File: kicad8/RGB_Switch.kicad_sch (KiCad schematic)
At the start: 0 parts

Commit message: Added: Stepped CAPS_LOCK and Split backspace
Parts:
- added Q1: WSD4070DN, PCM_marbastlib-various:PDFN3.3x3.3_EP, symbol PCM_marbastlib-various:WSD4070DN
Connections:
- new net: Q1.1 (S), Q1.2 (S), Q1.3 (S)
- new net: Q1.5 (D), Q1.6 (D), Q1.7 (D), Q1.8 (D), Q1.9 (D)
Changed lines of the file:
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@@
 	(generator_version "8.0")
 	(paper "A4")
+	(symbol
+		(lib_id "PCM_marbastlib-various:WSD4070DN")
+		(at 33.02 26.67 0)
+		(unit 1)
+		(exclude_from_sim no)
+		(in_bom yes)
+		(on_board yes)
+		(dnp no)
+		(fields_autoplaced yes)
+		(property "Reference" "Q1"
+			(at 39.37 25.3999 0)
+			(effects
+				(font
+					(size 1.27 1.27)
+				)
+				(justify left)
+			)
+		)
+		(property "Value" "WSD4070DN"
+			(at 39.37 27.9399 0)
+			(effects
+				(font
+					(size 1.27 1.27)
+				)
+				(justify left)
+			)
+		)
+		(property "Footprint" "PCM_marbastlib-various:PDFN3.3x3.3_EP"
+			(at 38.1 24.13 0)
+			(effects
+				(font
+					(size 1.27 1.27)
+				)
+				(hide yes)
+			)
+		)
+		(property "Datasheet" "https://wmsc.lcsc.com/wmsc/upload/file/pdf/v2/lcsc/2008211234_Winsok-Semicon-WSD4070DN_C719095.pdf"
+			(at 33.02 39.37 0)
+			(effects
+				(font
+					(size 1.27 1.27)
+				)
+				(hide yes)
+			)
+		)
+		(property "Description" "NMOS 40V 4.5 mOhm 68A"
+			(at 33.02 26.67 0)
+			(effects
+				(font
+					(size 1.27 1.27)
+				)
+				(hide yes)
+			)
+		)
+		(pin "2"
+		)
+		(pin "3"
+		)
+		(pin "5"
+		)
+		(pin "4"
+		)
+		(pin "7"
+		)
+		(pin "1"
+		)
+		(pin "8"
+		)
+		(pin "6"
+		)
+		(pin "9"
+		)
+		(instances
+			(project ""
+				(path "/4d291fcf-fdf2-46ba-aa57-60bc75f9cc32/7638bbfc-5c02-4928-8821-3938de956d68"
+					(reference "Q1")
+					(unit 1)
+				)
+			)
+		)
+	)
 )

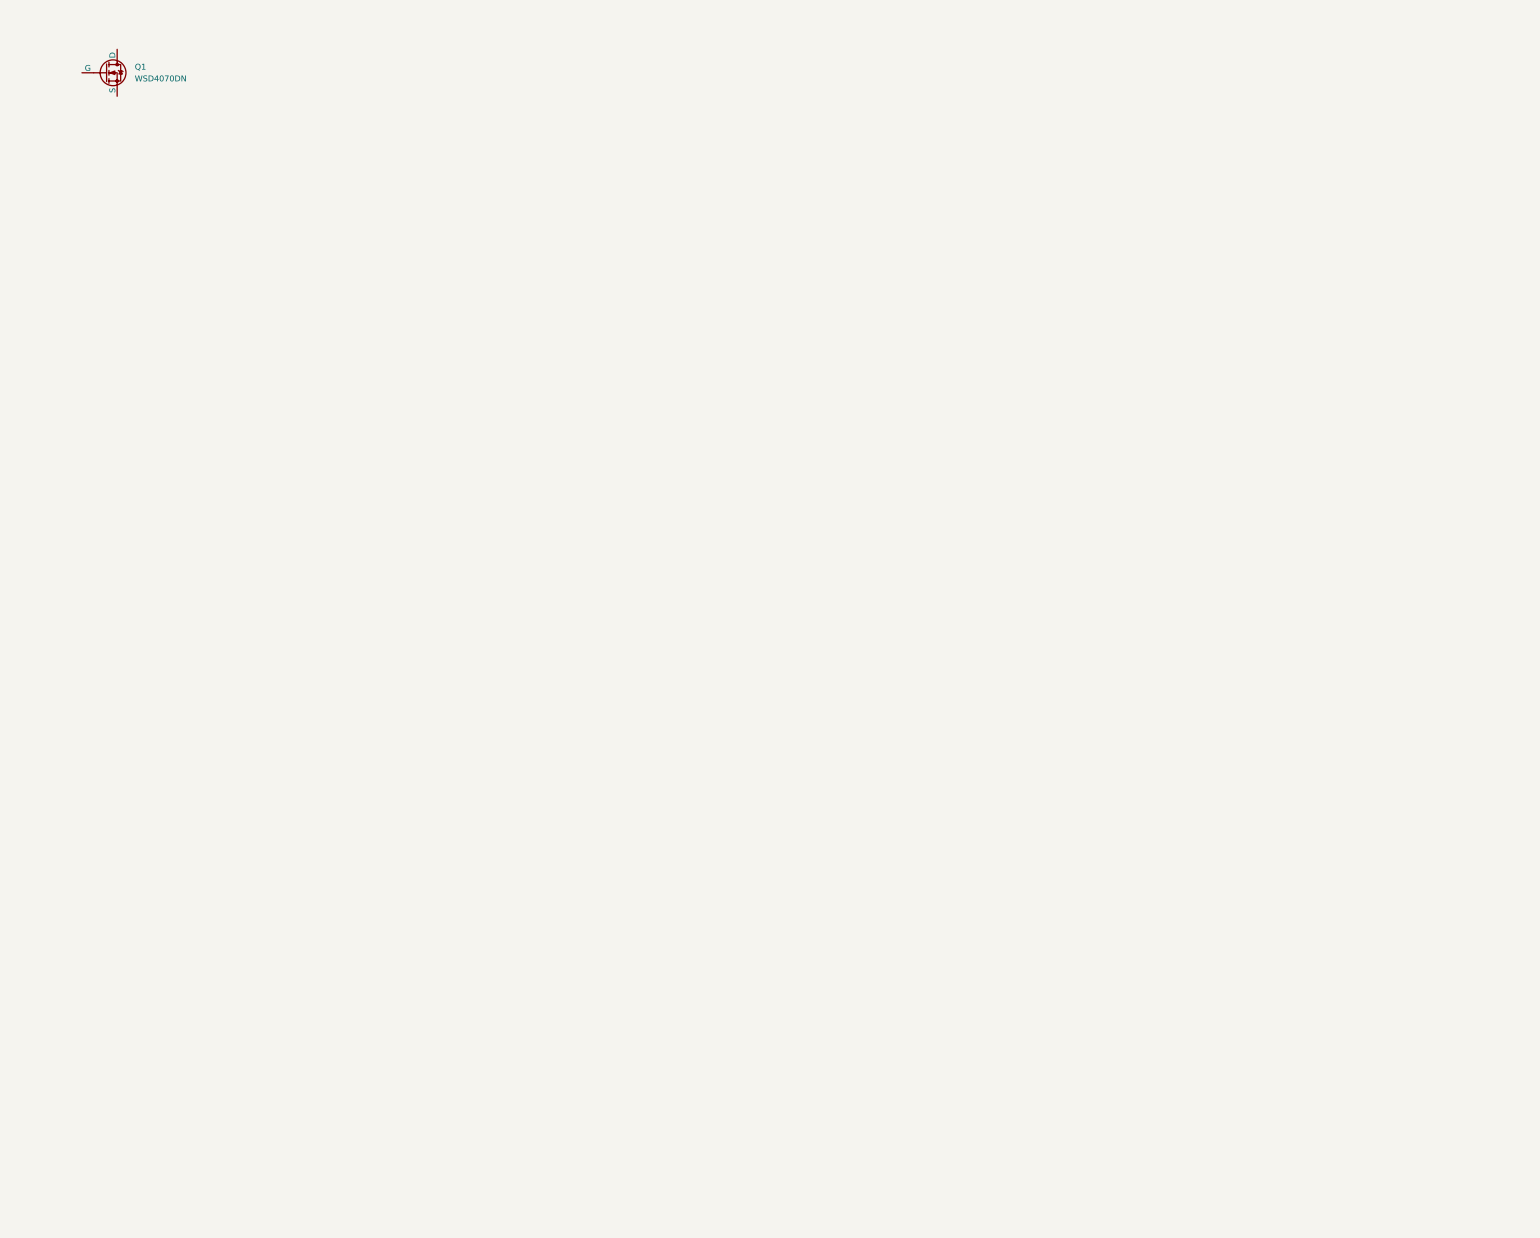
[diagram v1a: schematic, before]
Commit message: Finished: Wiring for the Switch matrix, Underglow RGB and Per-key RGb
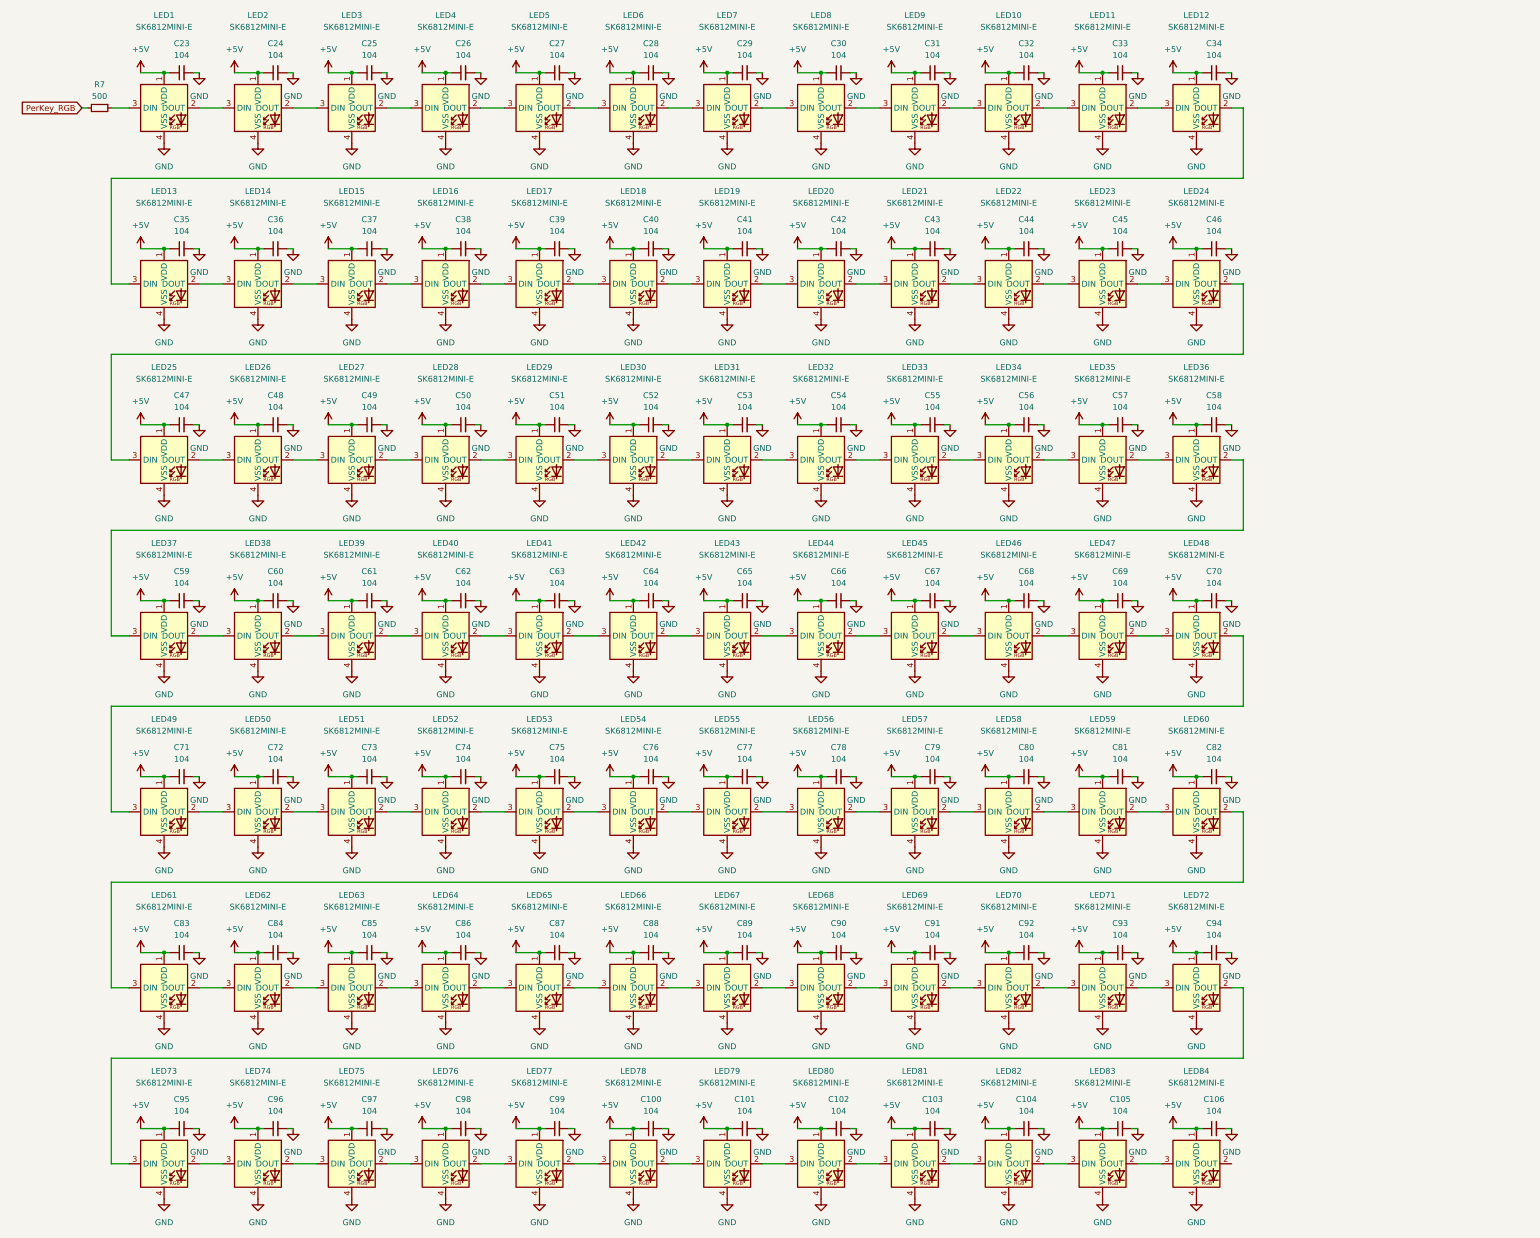
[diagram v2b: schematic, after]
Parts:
- removed Q1: WSD4070DN, PCM_marbastlib-various:PDFN3.3x3.3_EP, symbol PCM_marbastlib-various:WSD4070DN
- added C100, C101, C102, C103, C104, C105, C106, C23, C24, C25, C26, C27, C28, C29, C30, C31, C32, C33, C34, C35, C36, C37, C38, C39, C40, C41, C42, C43, C44, C45, C46, C47, C48, C49, C50, C51, C52, C53, C54, C55, C56, C57, C58, C59, C60, C61, C62, C63, C64, C65, C66, C67, C68, C69, C70, C71, C72, C73, C74, C75, C76, C77, C78, C79, C80, C81, C82, C83, C84, C85, C86, C87, C88, C89, C90, C91, C92, C93, C94, C95, C96, C97, C98, C99: 104, Diode_SMD:D_SOD-123, symbol Device:C_Small
- added LED1, LED10, LED11, LED12, LED13, LED14, LED15, LED16, LED17, LED18, LED19, LED2, LED20, LED21, LED22, LED23, LED24, LED25, LED26, LED27, LED28, LED29, LED3, LED30, LED31, LED32, LED33, LED34, LED35, LED36, LED37, LED38, LED39, LED4, LED40, LED41, LED42, LED43, LED44, LED45, LED46, LED47, LED48, LED49, LED5, LED50, LED51, LED52, LED53, LED54, LED55, LED56, LED57, LED58, LED59, LED6, LED60, LED61, LED62, LED63, LED64, LED65, LED66, LED67, LED68, LED69, LED7, LED70, LED71, LED72, LED73, LED74, LED75, LED76, LED77, LED78, LED79, LED8, LED80, LED81, LED82, LED83, LED84, LED9: SK6812MINI-E, PCM_marbastlib-various:LED_6028R, symbol PCM_marbastlib-various:SK6812MINI-E
- added R7: 500, Diode_SMD:D_SOD-123, symbol Device:R_Small
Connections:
- new net: LED73.2 (DOUT), LED74.3 (DIN)
- new net: LED72.2 (DOUT), LED73.3 (DIN)
- new net: LED45.2 (DOUT), LED46.3 (DIN)
- new net: LED44.2 (DOUT), LED45.3 (DIN)
- new net: LED79.2 (DOUT), LED80.3 (DIN)
- new net: LED78.2 (DOUT), LED79.3 (DIN)
- new net: LED42.2 (DOUT), LED43.3 (DIN)
- new net: LED41.2 (DOUT), LED42.3 (DIN)
- new net: LED35.2 (DOUT), LED36.3 (DIN)
- new net: LED34.2 (DOUT), LED35.3 (DIN)
- new net: LED15.2 (DOUT), LED16.3 (DIN)
- new net: LED14.2 (DOUT), LED15.3 (DIN)
- new net: LED5.2 (DOUT), LED6.3 (DIN)
- new net: LED4.2 (DOUT), LED5.3 (DIN)
- new net: LED37.2 (DOUT), LED38.3 (DIN)
- new net: LED36.2 (DOUT), LED37.3 (DIN)
- new net: LED17.2 (DOUT), LED18.3 (DIN)
- new net: LED16.2 (DOUT), LED17.3 (DIN)
- new net: LED50.2 (DOUT), LED51.3 (DIN)
- new net: LED49.2 (DOUT), LED50.3 (DIN)
- new net: LED74.2 (DOUT), LED75.3 (DIN)
- new net: LED48.2 (DOUT), LED49.3 (DIN)
- new net: LED47.2 (DOUT), LED48.3 (DIN)
- new net: LED38.2 (DOUT), LED39.3 (DIN)
- new net: LED75.2 (DOUT), LED76.3 (DIN)
- new net: LED81.2 (DOUT), LED82.3 (DIN)
- new net: LED80.2 (DOUT), LED81.3 (DIN)
- new net: LED23.2 (DOUT), LED24.3 (DIN)
- new net: LED22.2 (DOUT), LED23.3 (DIN)
- new net: LED70.2 (DOUT), LED71.3 (DIN)
- new net: LED69.2 (DOUT), LED70.3 (DIN)
- new net: LED66.2 (DOUT), LED67.3 (DIN)
- new net: LED65.2 (DOUT), LED66.3 (DIN)
- new net: LED10.2 (DOUT), LED11.3 (DIN)
- new net: LED10.3 (DIN), LED9.2 (DOUT)
- new net: LED57.2 (DOUT), LED58.3 (DIN)
- new net: LED56.2 (DOUT), LED57.3 (DIN)
- new net: LED67.2 (DOUT), LED68.3 (DIN)
- new net: LED53.2 (DOUT), LED54.3 (DIN)
- new net: LED52.2 (DOUT), LED53.3 (DIN)
- new net: LED63.2 (DOUT), LED64.3 (DIN)
- new net: LED62.2 (DOUT), LED63.3 (DIN)
- new net: LED60.2 (DOUT), LED61.3 (DIN)
- new net: LED59.2 (DOUT), LED60.3 (DIN)
- new net: LED25.2 (DOUT), LED26.3 (DIN)
- new net: LED24.2 (DOUT), LED25.3 (DIN)
- new net: LED8.2 (DOUT), LED9.3 (DIN)
- new net: LED7.2 (DOUT), LED8.3 (DIN)
- new net: LED40.2 (DOUT), LED41.3 (DIN)
- new net: LED39.2 (DOUT), LED40.3 (DIN)
- new net: LED13.2 (DOUT), LED14.3 (DIN)
- new net: LED20.2 (DOUT), LED21.3 (DIN)
- new net: LED19.2 (DOUT), LED20.3 (DIN)
- new net: LED82.2 (DOUT), LED83.3 (DIN)
- new net: LED3.2 (DOUT), LED4.3 (DIN)
- new net: LED54.2 (DOUT), LED55.3 (DIN)
- new net: LED6.2 (DOUT), LED7.3 (DIN)
- new net: LED51.2 (DOUT), LED52.3 (DIN)
- new net: LED28.2 (DOUT), LED29.3 (DIN)
- new net: LED27.2 (DOUT), LED28.3 (DIN)
- new net: LED33.2 (DOUT), LED34.3 (DIN)
- new net: LED32.2 (DOUT), LED33.3 (DIN)
- new net: LED29.2 (DOUT), LED30.3 (DIN)
- new net: LED31.2 (DOUT), LED32.3 (DIN)
- new net: LED46.2 (DOUT), LED47.3 (DIN)
- new net: LED64.2 (DOUT), LED65.3 (DIN)
- new net: LED12.2 (DOUT), LED13.3 (DIN)
- new net: LED1.2 (DOUT), LED2.3 (DIN)
- new net: LED1.3 (DIN), R7.1
- new net: LED83.2 (DOUT), LED84.3 (DIN)
- new net: LED26.2 (DOUT), LED27.3 (DIN)
- new net: LED76.2 (DOUT), LED77.3 (DIN)
- new net: LED2.2 (DOUT), LED3.3 (DIN)
- new net: LED61.2 (DOUT), LED62.3 (DIN)
- new net: LED30.2 (DOUT), LED31.3 (DIN)
- new net: LED68.2 (DOUT), LED69.3 (DIN)
- new net: LED71.2 (DOUT), LED72.3 (DIN)
- new net: LED43.2 (DOUT), LED44.3 (DIN)
- new net: LED18.2 (DOUT), LED19.3 (DIN)
- new net: LED21.2 (DOUT), LED22.3 (DIN)
- new net: LED55.2 (DOUT), LED56.3 (DIN)
- new net: LED11.2 (DOUT), LED12.3 (DIN)
- new net: LED77.2 (DOUT), LED78.3 (DIN)
- new net: LED58.2 (DOUT), LED59.3 (DIN)
- new net +5V: C100.1, C101.1, C102.1, C103.1, C104.1, C105.1, C106.1, C23.1, C24.1, C25.1, C26.1, C27.1, C28.1, C29.1, C30.1, C31.1, C32.1, C33.1, C34.1, C35.1, C36.1, C37.1, C38.1, C39.1, C40.1, C41.1, C42.1, C43.1, C44.1, C45.1, C46.1, C47.1, C48.1, C49.1, C50.1, C51.1, C52.1, C53.1, C54.1, C55.1, C56.1, C57.1, C58.1, C59.1, C60.1, C61.1, C62.1, C63.1, C64.1, C65.1, C66.1, C67.1, C68.1, C69.1, C70.1, C71.1, C72.1, C73.1, C74.1, C75.1, C76.1, C77.1, C78.1, C79.1, C80.1, C81.1, C82.1, C83.1, C84.1, C85.1, C86.1, C87.1, C88.1, C89.1, C90.1, C91.1, C92.1, C93.1, C94.1, C95.1, C96.1, C97.1, C98.1, C99.1, LED1.1 (VDD), LED10.1 (VDD), LED11.1 (VDD), LED12.1 (VDD), LED13.1 (VDD), LED14.1 (VDD), LED15.1 (VDD), LED16.1 (VDD), LED17.1 (VDD), LED18.1 (VDD), LED19.1 (VDD), LED2.1 (VDD), LED20.1 (VDD), LED21.1 (VDD), LED22.1 (VDD), LED23.1 (VDD), LED24.1 (VDD), LED25.1 (VDD), LED26.1 (VDD), LED27.1 (VDD), LED28.1 (VDD), LED29.1 (VDD), LED3.1 (VDD), LED30.1 (VDD), LED31.1 (VDD), LED32.1 (VDD), LED33.1 (VDD), LED34.1 (VDD), LED35.1 (VDD), LED36.1 (VDD), LED37.1 (VDD), LED38.1 (VDD), LED39.1 (VDD), LED4.1 (VDD), LED40.1 (VDD), LED41.1 (VDD), LED42.1 (VDD), LED43.1 (VDD), LED44.1 (VDD), LED45.1 (VDD), LED46.1 (VDD), LED47.1 (VDD), LED48.1 (VDD), LED49.1 (VDD), LED5.1 (VDD), LED50.1 (VDD), LED51.1 (VDD), LED52.1 (VDD), LED53.1 (VDD), LED54.1 (VDD), LED55.1 (VDD), LED56.1 (VDD), LED57.1 (VDD), LED58.1 (VDD), LED59.1 (VDD), LED6.1 (VDD), LED60.1 (VDD), LED61.1 (VDD), LED62.1 (VDD), LED63.1 (VDD), LED64.1 (VDD), LED65.1 (VDD), LED66.1 (VDD), LED67.1 (VDD), LED68.1 (VDD), LED69.1 (VDD), LED7.1 (VDD), LED70.1 (VDD), LED71.1 (VDD), LED72.1 (VDD), LED73.1 (VDD), LED74.1 (VDD), LED75.1 (VDD), LED76.1 (VDD), LED77.1 (VDD), LED78.1 (VDD), LED79.1 (VDD), LED8.1 (VDD), LED80.1 (VDD), LED81.1 (VDD), LED82.1 (VDD), LED83.1 (VDD), LED84.1 (VDD), LED9.1 (VDD)
- new net GND: C100.2, C101.2, C102.2, C103.2, C104.2, C105.2, C106.2, C23.2, C24.2, C25.2, C26.2, C27.2, C28.2, C29.2, C30.2, C31.2, C32.2, C33.2, C34.2, C35.2, C36.2, C37.2, C38.2, C39.2, C40.2, C41.2, C42.2, C43.2, C44.2, C45.2, C46.2, C47.2, C48.2, C49.2, C50.2, C51.2, C52.2, C53.2, C54.2, C55.2, C56.2, C57.2, C58.2, C59.2, C60.2, C61.2, C62.2, C63.2, C64.2, C65.2, C66.2, C67.2, C68.2, C69.2, C70.2, C71.2, C72.2, C73.2, C74.2, C75.2, C76.2, C77.2, C78.2, C79.2, C80.2, C81.2, C82.2, C83.2, C84.2, C85.2, C86.2, C87.2, C88.2, C89.2, C90.2, C91.2, C92.2, C93.2, C94.2, C95.2, C96.2, C97.2, C98.2, C99.2, LED1.4 (VSS), LED10.4 (VSS), LED11.4 (VSS), LED12.4 (VSS), LED13.4 (VSS), LED14.4 (VSS), LED15.4 (VSS), LED16.4 (VSS), LED17.4 (VSS), LED18.4 (VSS), LED19.4 (VSS), LED2.4 (VSS), LED20.4 (VSS), LED21.4 (VSS), LED22.4 (VSS), LED23.4 (VSS), LED24.4 (VSS), LED25.4 (VSS), LED26.4 (VSS), LED27.4 (VSS), LED28.4 (VSS), LED29.4 (VSS), LED3.4 (VSS), LED30.4 (VSS), LED31.4 (VSS), LED32.4 (VSS), LED33.4 (VSS), LED34.4 (VSS), LED35.4 (VSS), LED36.4 (VSS), LED37.4 (VSS), LED38.4 (VSS), LED39.4 (VSS), LED4.4 (VSS), LED40.4 (VSS), LED41.4 (VSS), LED42.4 (VSS), LED43.4 (VSS), LED44.4 (VSS), LED45.4 (VSS), LED46.4 (VSS), LED47.4 (VSS), LED48.4 (VSS), LED49.4 (VSS), LED5.4 (VSS), LED50.4 (VSS), LED51.4 (VSS), LED52.4 (VSS), LED53.4 (VSS), LED54.4 (VSS), LED55.4 (VSS), LED56.4 (VSS), LED57.4 (VSS), LED58.4 (VSS), LED59.4 (VSS), LED6.4 (VSS), LED60.4 (VSS), LED61.4 (VSS), LED62.4 (VSS), LED63.4 (VSS), LED64.4 (VSS), LED65.4 (VSS), LED66.4 (VSS), LED67.4 (VSS), LED68.4 (VSS), LED69.4 (VSS), LED7.4 (VSS), LED70.4 (VSS), LED71.4 (VSS), LED72.4 (VSS), LED73.4 (VSS), LED74.4 (VSS), LED75.4 (VSS), LED76.4 (VSS), LED77.4 (VSS), LED78.4 (VSS), LED79.4 (VSS), LED8.4 (VSS), LED80.4 (VSS), LED81.4 (VSS), LED82.4 (VSS), LED83.4 (VSS), LED84.4 (VSS), LED9.4 (VSS)
- new net PerKey_RGB: R7.2

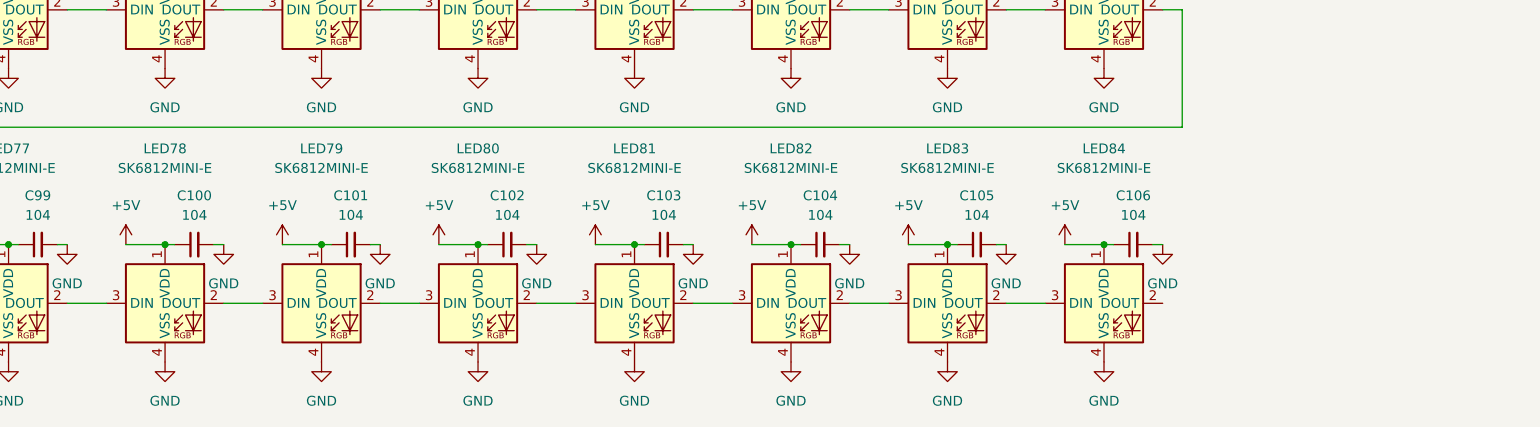
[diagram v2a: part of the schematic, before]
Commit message: Added: more ground fill vias and split space bars
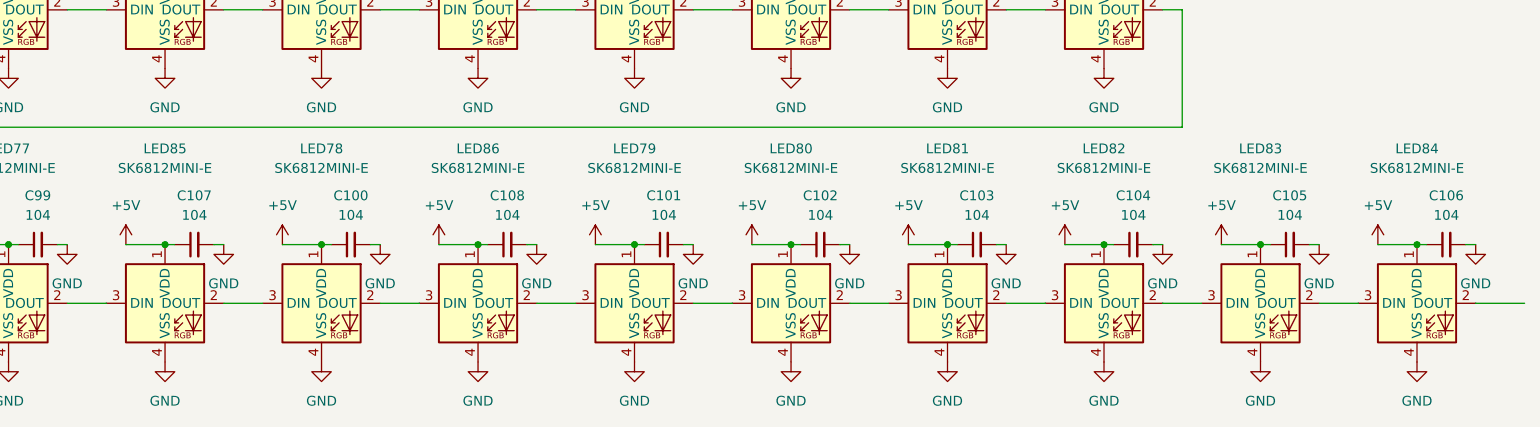
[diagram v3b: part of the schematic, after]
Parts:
- added C107, C108: 104, Diode_SMD:D_SOD-123, symbol Device:C_Small
- added LED85, LED86: SK6812MINI-E, PCM_marbastlib-various:LED_6028R, symbol PCM_marbastlib-various:SK6812MINI-E
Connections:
- net +5V: now also C107.1, C108.1, LED85.1 (VDD), LED86.1 (VDD)
- net GND: now also C107.2, C108.2, LED85.4 (VSS), LED86.4 (VSS)
- net at LED79.3 (DIN): now also LED86.2 (DOUT); no longer LED78.2 (DOUT)
- net at LED78.3 (DIN): now also LED85.2 (DOUT); no longer LED77.2 (DOUT)
- new net: LED78.2 (DOUT), LED86.3 (DIN)
- new net: LED77.2 (DOUT), LED85.3 (DIN)
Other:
- moved on the sheet: C100, C101, C102, C103, C104, C105, C106, LED78, LED79, LED80, LED81, LED82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

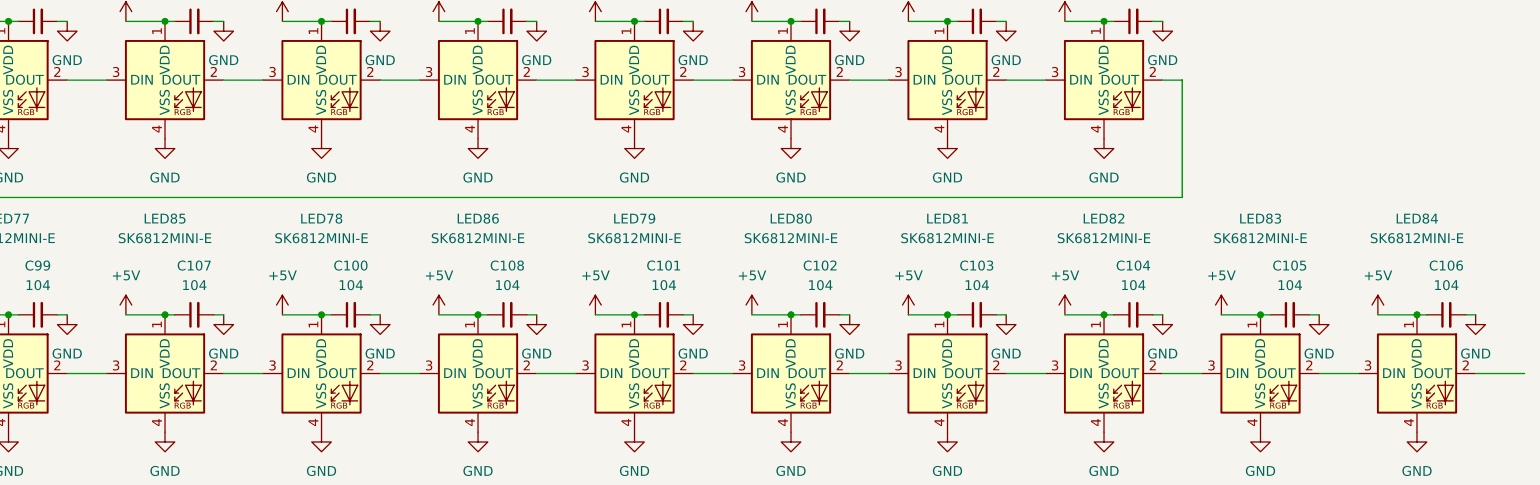
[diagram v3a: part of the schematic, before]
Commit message: Fixed: Silkscreens overlap
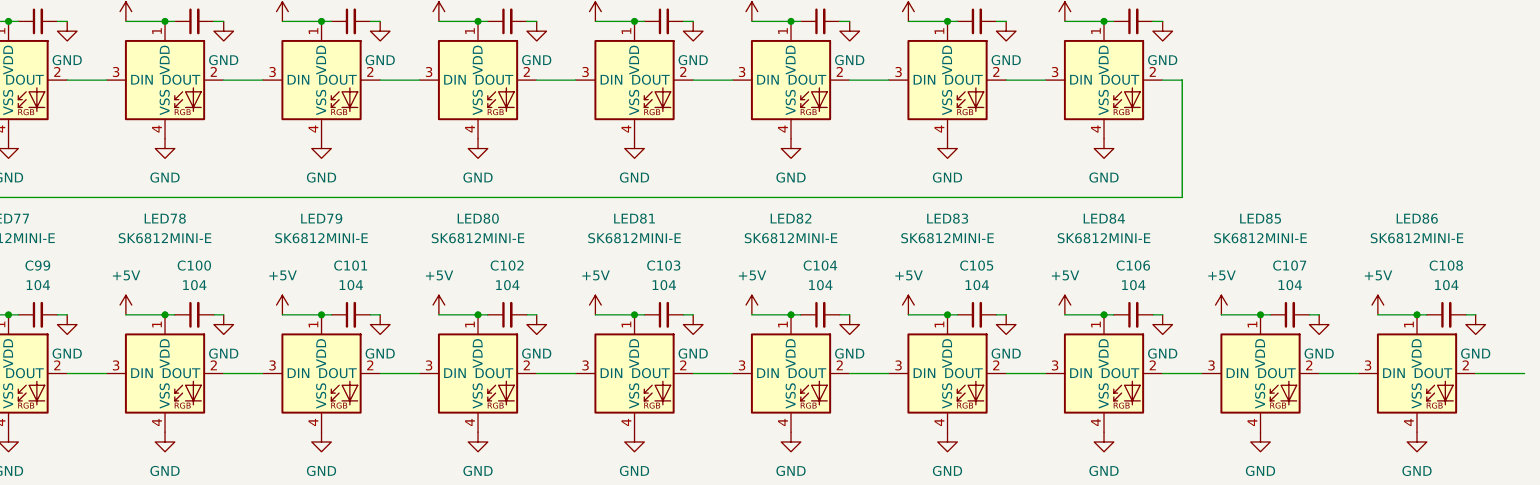
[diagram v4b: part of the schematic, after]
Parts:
- renumbered C107 to C100, C100 to C101, C108 to C102, C101 to C103, C102 to C104, C103 to C105, C104 to C106, C105 to C107, C106 to C108, LED85 to LED78, LED78 to LED79, LED86 to LED80, LED79 to LED81, LED80 to LED82, LED81 to LED83, LED82 to LED84, LED83 to LED85, LED84 to LED86

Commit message: Removed: old RGB file
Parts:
- C100, C101, C102, C103, C104, C105, C106, C107, C108, C23, C24, C25, C26, C27, C28, C29, C30, C31, C32, C33, C34, C35, C36, C37, C38, C39, C40, C41, C42, C43, C44, C45, C46, C47, C48, C49, C50, C51, C52, C53, C54, C55, C56, C57, C58, C59, C60, C61, C62, C63, C64, C65, C66, C67, C68, C69, C70, C71, C72, C73, C74, C75, C76, C77, C78, C79, C80, C81, C82, C83, C84, C85, C86, C87, C88, C89, C90, C91, C92, C93, C94, C95, C96, C97, C98, C99: footprint Diode_SMD:D_SOD-123 -> Capacitor_SMD:C_0402_1005Metric

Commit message: Initial branch commit
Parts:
- R7: footprint Diode_SMD:D_SOD-123 -> Resistor_SMD:R_0402_1005Metric
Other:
- moved on the sheet: C100, C101, C102, C103, C104, C105, C106, C107, C108, C35, C36, C37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
